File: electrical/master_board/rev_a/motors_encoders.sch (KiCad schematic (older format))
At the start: 7 parts, among them CN91 HR2_ENCODER;2xF1x3, CN92 HR2_ENCODER;2xF1x3, U4 DRV8833PWPR;16HTSSOP

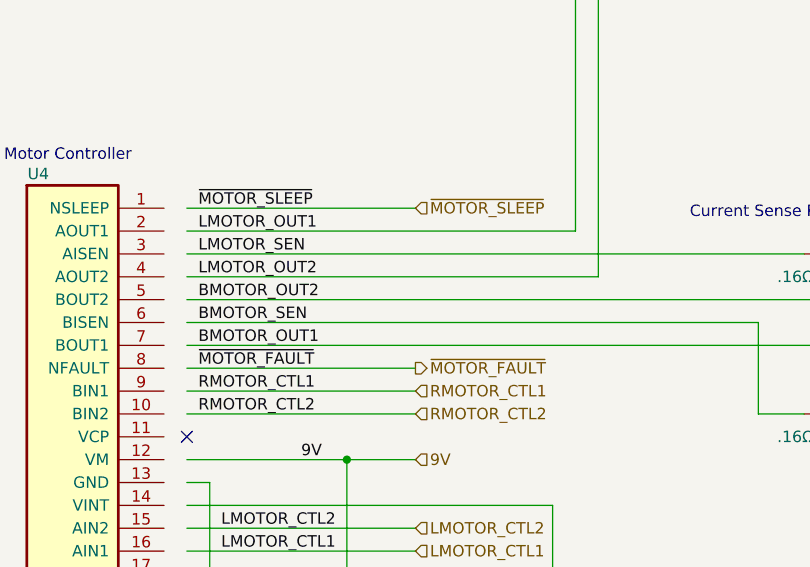
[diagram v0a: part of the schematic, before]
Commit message: Updated WOWBus portion of schematic.
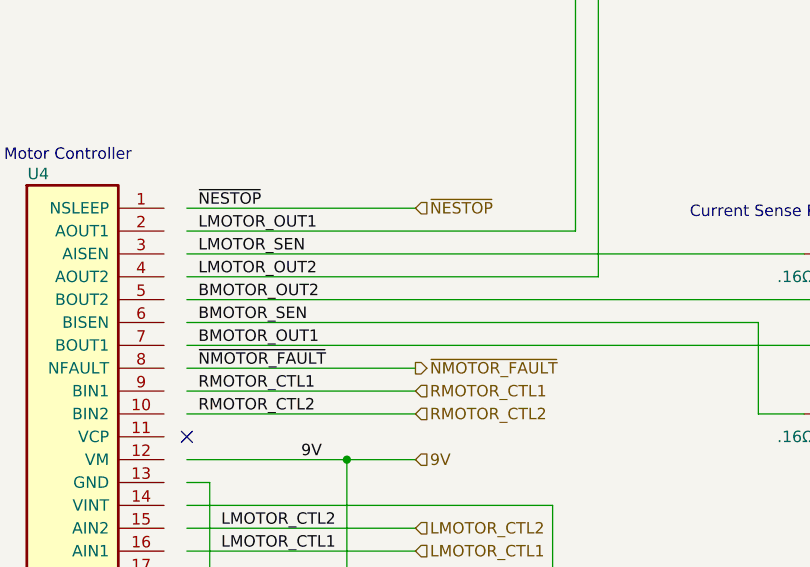
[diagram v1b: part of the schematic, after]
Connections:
- net labels added: ~NESTOP, ~NMOTOR_FAULT
- net labels removed: ~MOTOR_FAULT, ~MOTOR_SLEEP
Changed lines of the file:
@@
 	3200 3500 4200 3500
 Text HLabel 4200 3500 2    50   Input ~ 0
-~MOTOR_SLEEP
+~NESTOP
 Text Label 3250 3500 0    50   ~ 0
-~MOTOR_SLEEP
+~NESTOP
 Text HLabel 4200 4200 2    50   Output ~ 0
-~MOTOR_FAULT
+~NMOTOR_FAULT
 Wire Wire Line
 	3200 4200 4200 4200
 Text Label 3250 4200 0    50   ~ 0
-~MOTOR_FAULT
+~NMOTOR_FAULT
 Wire Wire Line
 	3200 3600 4900 3600

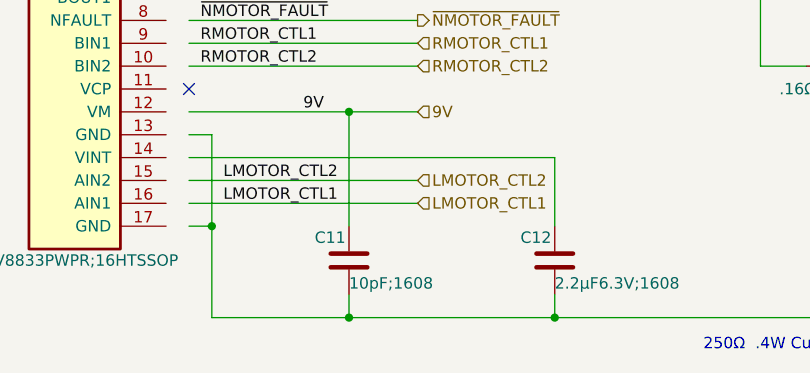
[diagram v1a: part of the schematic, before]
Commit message: Added RC filter to servo current sense.
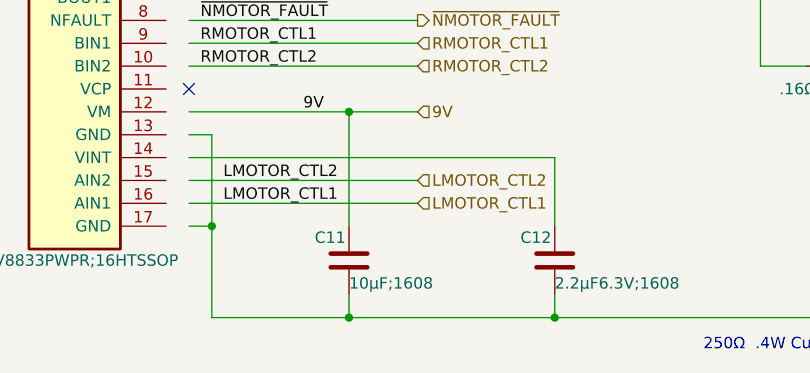
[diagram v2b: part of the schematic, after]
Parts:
- C11: value 10pF;1608 -> 10µF;1608
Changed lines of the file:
@@
 P 3900 5250
 F 0 "C11" H 3750 5350 50  0000 L CNN
-F 1 "10pF;1608" H 3900 5150 50  0000 L CNN
+F 1 "10µF;1608" H 3900 5150 50  0000 L CNN
 F 2 "Capacitor_SMD:C_0603_1608Metric" H 3938 5100 50  0001 C CNN
 F 3 "~" H 3900 5250 50  0001 C CNN

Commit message: JLCPCB Footprints are both consistent and available.
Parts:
- removed U4: DRV8833PWPR;16HTSSOP, Package_SO:HTSSOP-16-1EP_4.4x5mm_P0.65mm_EP3.4x5mm_Mask3x3mm_ThermalVias, symbol HR2:DRV8833PWPR;16HTSSOP
- added U4: DRV8833PWPR;HTSSOP16EP3.4x5, Package_SO:HTSSOP-16-1EP_4.4x5mm_P0.65mm_EP3.4x5mm_Mask3x3mm_ThermalVias, symbol HR2:DRV8833PWPR;HTSSOP16EP3.4x5
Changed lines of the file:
@@
 Text HLabel 4200 5000 2    50   Input ~ 0
 LMOTOR_CTL1
-$Comp
-L HR2:DRV8833PWPR;16HTSSOP U4
-U 1 1 5F4C0C8C
-P 2300 3500
-F 0 "U4" H 2550 3650 50  0000 C CNN
-F 1 "DRV8833PWPR;16HTSSOP" H 2700 1750 50  0000 C CNN
-F 2 "Package_SO:HTSSOP-16-1EP_4.4x5mm_P0.65mm_EP3.4x5mm_Mask3x3mm_ThermalVias" H 2500 3550 60  0001 L CNN
-F 3 "Dual H-Bridge Motor Drive" H 2500 3350 60  0001 L CNN
-F 4 "DualH-Bridge Motor Drive" H 2500 3250 60  0001 L CNN "Field5"
-	1    2300 3500
-	1    0    0    -1
-$EndComp
 Wire Wire Line
 	3200 5000 4200 5000
@@
 NoConn ~ 3200 4500
 NoConn ~ 6500 1450
+$Comp
+L HR2:DRV8833PWPR;HTSSOP16EP3.4x5 U4
+U 1 1 5FE0E792
+P 2300 3500
+F 0 "U4" H 2550 3650 50  0000 C CNN
+F 1 "DRV8833PWPR;HTSSOP16EP3.4x5" H 2550 1750 50  0000 C CNN
+F 2 "Package_SO:HTSSOP-16-1EP_4.4x5mm_P0.65mm_EP3.4x5mm_Mask3x3mm_ThermalVias" H 2500 3550 60  0001 L CNN
+F 3 "Dual H-Bridge Motor Drive" H 2500 3350 60  0001 L CNN
+F 4 "DualH-Bridge Motor Drive" H 2500 3250 60  0001 L CNN "desc"
+	1    2300 3500
+	1    0    0    -1
+$EndComp
 $EndSCHEMATC

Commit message: Switched Encoders to 5V.
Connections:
- net labels added: 5V
- net labels removed: 3.3V
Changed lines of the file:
@@
 Wire Wire Line
 	3200 3900 6900 3900
-Text HLabel 8300 3300 2    50   Input ~ 0
-3.3V
 Text HLabel 8300 2900 2    50   Output ~ 0
 LQUAD_B
@@
 Wire Wire Line
 	6800 4400 6900 4400
-Text Label 7300 3300 2    50   ~ 0
-3.3V
+Text Label 8300 3300 2    50   ~ 0
+5V
 Text Label 8300 5000 2    50   ~ 0
 RQUAD_A
 Text Label 8300 4900 2    50   ~ 0
 RQUAD_B
-Text Label 7300 3000 2    50   ~ 0
+Text Label 8300 3000 2    50   ~ 0
 LQUAD_A
-Text Label 7300 2900 2    50   ~ 0
+Text Label 8300 2900 2    50   ~ 0
 LQUAD_B
 Text Label 3700 4600 0    50   ~ 0
@@
 	1    0    0    -1
 $EndComp
+Text HLabel 8300 3300 2    50   Input ~ 0
+5V
 $EndSCHEMATC

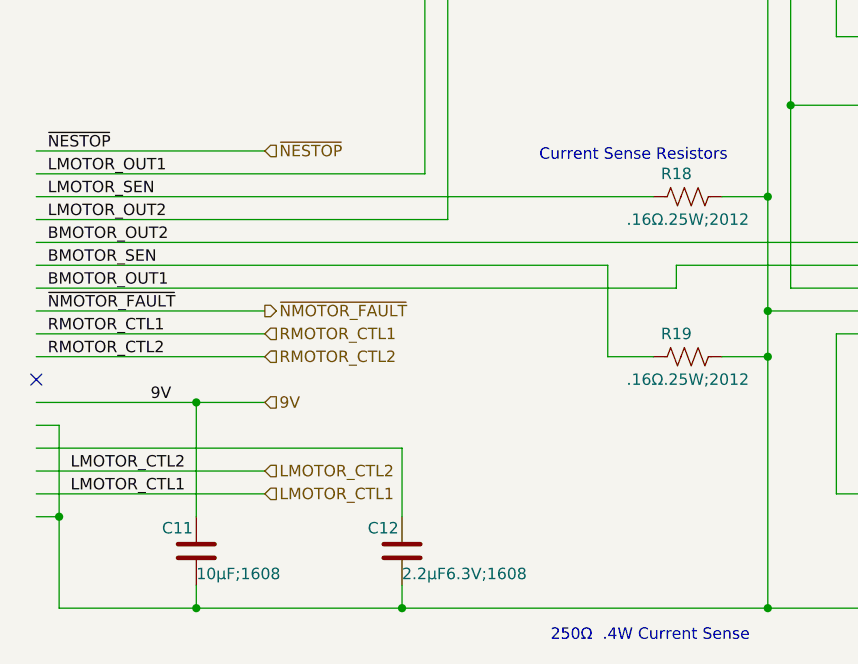
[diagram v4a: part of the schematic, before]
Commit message: Reannoated schematic symbols.
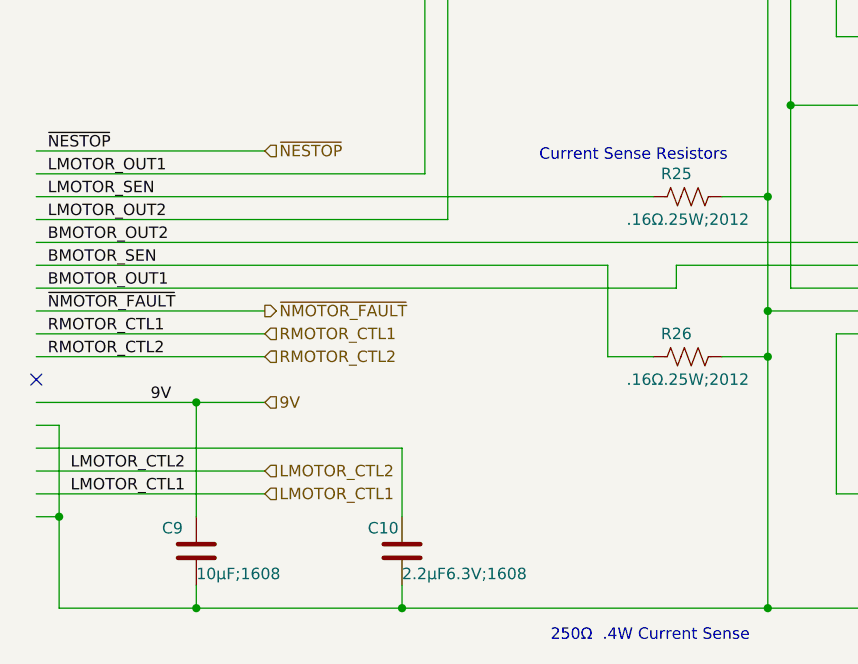
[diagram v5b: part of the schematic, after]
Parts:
- renumbered C12 to C10, C11 to C9, CN92 to CN6, CN91 to CN7, R18 to R25, R19 to R26, U4 to U6
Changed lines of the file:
@@
 	3200 5000 4200 5000
 $Comp
-L Device:C C12
+L Device:C C10
 U 1 1 5F4CB112
 P 4800 5250
-F 0 "C12" H 4650 5350 50  0000 L CNN
+F 0 "C10" H 4650 5350 50  0000 L CNN
 F 1 "2.2µF6.3V;1608" H 4800 5150 50  0000 L CNN
 F 2 "Capacitor_SMD:C_0603_1608Metric" H 4838 5100 50  0001 C CNN
@@
 	6200 3700 6400 3700
 $Comp
-L Device:R_US R18
+L Device:R_US R25
 U 1 1 5F4CC3F2
 P 6050 3700
-F 0 "R18" V 5950 3650 50  0000 C CNN
+F 0 "R25" V 5950 3650 50  0000 C CNN
 F 1 ".16Ω.25W;2012" V 6150 3700 50  0000 C CNN
 F 2 "Resistor_SMD:R_0805_2012Metric" V 6090 3690 50  0001 C CNN
@@
 Left Motor/Encoder\nConnectors
 $Comp
-L Device:C C11
+L Device:C C9
 U 1 1 5FA19E5E
 P 3900 5250
-F 0 "C11" H 3750 5350 50  0000 L CNN
+F 0 "C9" H 3750 5350 50  0000 L CNN
 F 1 "10µF;1608" H 3900 5150 50  0000 L CNN
 F 2 "Capacitor_SMD:C_0603_1608Metric" H 3938 5100 50  0001 C CNN
@@
 	3900 5500 4800 5500
 $Comp
-L HR2:ENCODER;2xF1x3 CN92
+L HR2:ENCODER;2xF1x3 CN6
 U 1 1 5F967601
 P 7800 2000
-F 0 "CN92" H 8500 2150 50  0000 R CNN
+F 0 "CN6" H 8500 2150 50  0000 R CNN
 F 1 "HR2_ENCODER;2xF1x3" H 8650 1350 50  0000 R CNN
 F 2 "HR2:ENCODER_2xF1x3" H 8000 2050 60  0001 L CNN
@@
 $EndComp
 $Comp
-L HR2:ENCODER;2xF1x3 CN91
+L HR2:ENCODER;2xF1x3 CN7
 U 1 1 5F968E59
 P 7800 3900
-F 0 "CN91" H 8500 4050 50  0000 R CNN
+F 0 "CN7" H 8500 4050 50  0000 R CNN
 F 1 "HR2_ENCODER;2xF1x3" H 8650 3250 50  0000 R CNN
 F 2 "HR2:ENCODER_2xF1x3" H 8000 3950 60  0001 L CNN
@@
 	6400 4400 6400 5500
 $Comp
-L Device:R_US R19
+L Device:R_US R26
 U 1 1 5FA3CBD5
 P 6050 4400
-F 0 "R19" V 5950 4350 50  0000 C CNN
+F 0 "R26" V 5950 4350 50  0000 C CNN
 F 1 ".16Ω.25W;2012" V 6150 4400 50  0000 C CNN
 F 2 "Resistor_SMD:R_0805_2012Metric" V 6090 4390 50  0001 C CNN
@@
 NoConn ~ 6500 1450
 $Comp
-L HR2:DRV8833PWPR;HTSSOP16EP3.4x5 U4
+L HR2:DRV8833PWPR;HTSSOP16EP3.4x5 U6
 U 1 1 5FE0E792
 P 2300 3500
-F 0 "U4" H 2550 3650 50  0000 C CNN
+F 0 "U6" H 2550 3650 50  0000 C CNN
 F 1 "DRV8833PWPR;HTSSOP16EP3.4x5" H 2550 1750 50  0000 C CNN
 F 2 "Package_SO:HTSSOP-16-1EP_4.4x5mm_P0.65mm_EP3.4x5mm_Mask3x3mm_ThermalVias" H 2500 3550 60  0001 L CNN
